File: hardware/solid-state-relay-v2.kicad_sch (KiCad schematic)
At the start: 17 parts

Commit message: fix schematic library
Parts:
- C1: value (none) -> 220pF; footprint (none) -> kicad-libraries:C0402F; symbol C -> tinkerforge:C
- C2: value (none) -> 10uF; footprint (none) -> kicad-libraries:C0805; symbol C -> tinkerforge:C
- C3: value (none) -> 1uF; footprint (none) -> kicad-libraries:C0603F; symbol C -> tinkerforge:C
- C4: value (none) -> 100nF; footprint (none) -> kicad-libraries:C0603F; symbol C -> tinkerforge:C
- D1: value (none) -> blue; footprint (none) -> kicad-libraries:D0603F; symbol LED -> tinkerforge:LED
- P1: value (none) -> CON-SENSOR2; footprint (none) -> kicad-libraries:CON-SENSOR2; symbol CON-SENSOR2 -> tinkerforge:CON-SENSOR2
- P2, P3: value (none) -> TST; footprint (none) -> kicad-libraries:Drill; symbol TST -> tinkerforge:TST
- P5: value (none) -> BOOT; footprint (none) -> kicad-libraries:SolderJumper; symbol CONN_01X02 -> tinkerforge:CONN_01X02
- Q1: value (none) -> 2N7002P; footprint (none) -> kicad-libraries:SOT23GDS; symbol MOSFET_N_CH -> tinkerforge:MOSFET_N_CH
- R1: value (none) -> 10k; footprint (none) -> kicad-libraries:R0603F; symbol R -> tinkerforge:R
- R2, R3: value (none) -> 1k; footprint (none) -> kicad-libraries:R0603F; symbol R -> tinkerforge:R
- RP1: value (none) -> 82; footprint (none) -> kicad-libraries:4X0402; symbol R_PACK4 -> tinkerforge:R_PACK4
- U1: value (none) -> XMC110024; footprint (none) -> kicad-libraries:QFN24-4x4mm-0.5mm; symbol XMC1XXX24 -> tinkerforge:XMC1XXX24
- U2, U3: value (none) -> DRILL; footprint (none) -> kicad-libraries:DRILL_NP; symbol DRILL -> tinkerforge:DRILL
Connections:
- net S-CLK: now also RP1.7 (R2), U1.23 (P0.14_IO)
- net S-CS: now also RP1.8 (R1), U1.22 (P0.13_IO)
- net S-MISO: now also RP1.5 (R4), U1.1 (P2.0_AIO)
- net S-MOSI: now also RP1.6 (R3), U1.24 (P0.15_IO)
- net SSR: now also Q1.G, U1.13 (P1.1_IHO)
- new net: Q1.D, R2.2
- new net: P1.4, RP1.1 (P1)
- new net: P1.5, RP1.2 (P2)
- new net: P1.6, RP1.3 (P3)
- new net: C1.1, P1.7, RP1.4 (P4)
- new net: R3.1, U1.15 (P0.0_IO)
- new net: P5.2 (P2), U1.4 (P2.6_AI)
- new net: D1.2 (K), R3.2
- new net +5V: P1.1, R2.1
- new net GND: C1.2, C2.2, C3.2, C4.2, P1.2, P1.EP, P5.1 (P1), Q1.S, R1.2, U1.9 (VSSP/VSS), U1.EXP (VSSP)
- new net VCC: C2.1, C3.1, C4.1, D1.1 (A), P1.3, U1.10 (VDDP/VDD)

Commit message: Hardware 2.1: Made Pcb bigger to fit on the 40mm grid. Data Cleanup
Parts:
- P2: renamed from P3; symbol tinkerforge:TST -> tinkerforge:CONN_1
- P3: renamed from P2; symbol tinkerforge:TST -> tinkerforge:CONN_1
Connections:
- net +5V: now also P2.1
- net SSR: now also R1.1
- net at Q1.D, R2.2: now also P3.1
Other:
- note added: "Copyright Tinkerforge GmbH 2023. This documentation describes Open Hardware and is licensed under the CERN OHL v. 1.1. You may redistribute and modify this documentation under the terms of the CERN OHL v.1.1. (http://ohwr.org/cernohl). This documentation is distributed WITHOUT ANY EXPRESS OR IMPLIED WARRANTY, INCLUDING OF MERCHANTABILITY, SATISFACTORY QUALITY AND FITNESS FOR A PARTICULAR PURPOSE.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"
- note removed: "Copyright Tinkerforge GmbH 2017. This documentation describes Open Hardware and is licensed under the CERN OHL v. 1.1. You may redistribute and modify this documentation under the terms of the CERN OHL v.1.1. (http://ohwr.org/cernohl). This documentation is distributed WITHOUT ANY EXPRESS OR IMPLIED WARRANTY, INCLUDING OF MERCHANTABILITY, SATISFACTORY QUALITY AND FITNESS FOR A PARTICULAR PURPOSE.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"
- moved on the sheet: R1
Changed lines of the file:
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@@
   (title_block
     (title "Solid State Relay Bricklet")
-    (date "2017-09-18")
-    (rev "2.0")
+    (date "2023-01-27")
+    (rev "2.1")
     (company "Tinkerforge GmbH")
     (comment 1 "Licensed under CERN OHL v.1.1")
-    (comment 2 "Copyright (©) 2017, L.Lauer <lukas@tinkerforge.com>")
+    (comment 2 "Copyright (©) 2023, T.Schneidermann <tim@tinkerforge.com>")
   )
   (junction (at 57.15 20.32) (diameter 0) (color 0 0 0 0)
@@
   )
   (junction (at 40.64 45.72) (diameter 0) (color 0 0 0 0)
+  )
+  (junction (at 223.52 96.52) (diameter 0) (color 0 0 0 0)
   )
   (junction (at 100.33 181.61) (diameter 0) (color 0 0 0 0)
@@
     (stroke (width 0) (type default) (color 0 0 0 0))
   )
-  (wire (pts (xy 212.09 96.52) (xy 240.03 96.52))
+  (wire (pts (xy 212.09 96.52) (xy 223.52 96.52))
     (stroke (width 0) (type default) (color 0 0 0 0))
   )
@@
     (stroke (width 0) (type default) (color 0 0 0 0))
   )
-  (wire (pts (xy 224.79 110.49) (xy 224.79 109.22))
+  (wire (pts (xy 223.52 110.49) (xy 223.52 109.22))
     (stroke (width 0) (type default) (color 0 0 0 0))
   )
@@
     (stroke (width 0) (type default) (color 0 0 0 0))
   )
-  (wire (pts (xy 254 91.44) (xy 254 85.09))
+  (wire (pts (xy 254 91.44) (xy 254 87.63))
     (stroke (width 0) (type default) (color 0 0 0 0))
   )
@@
   )
   (wire (pts (xy 57.15 20.32) (xy 57.15 21.59))
+    (stroke (width 0) (type default) (color 0 0 0 0))
+  )
+  (wire (pts (xy 223.52 96.52) (xy 240.03 96.52))
     (stroke (width 0) (type default) (color 0 0 0 0))
   )
@@
     (effects (font (size 1.1938 1.1938)) (justify left bottom))
   )
-  (text "Copyright Tinkerforge GmbH 2017.\nThis documentation describes Open Hardware and is licensed under the\nCERN OHL v. 1.1.\nYou may redistribute and modify this documentation under the terms of the\nCERN OHL v.1.1. (http://ohwr.org/cernohl). This documentation is distributed\nWITHOUT ANY EXPRESS OR IMPLIED WARRANTY, INCLUDING OF\nMERCHANTABILITY, SATISFACTORY QUALITY AND FITNESS FOR A\nPARTICULAR PURPOSE. Please see the CERN OHL v.1.1 for applicable\nconditions\n"
+  (text "Copyright Tinkerforge GmbH 2023.\nThis documentation describes Open Hardware and is licensed under the\nCERN OHL v. 1.1.\nYou may redistribute and modify this documentation under the terms of the\nCERN OHL v.1.1. (http://ohwr.org/cernohl). This documentation is distributed\nWITHOUT ANY EXPRESS OR IMPLIED WARRANTY, INCLUDING OF\nMERCHANTABILITY, SATISFACTORY QUALITY AND FITNESS FOR A\nPARTICULAR PURPOSE. Please see the CERN OHL v.1.1 for applicable\nconditions\n"
     (at 12.7 196.85 0)
     (effects (font (size 1.016 1.016)) (justify left bottom))
@@
     (pin "1")
   )
-  (symbol (lib_id "tinkerforge:R") (at 224.79 102.87 0) (unit 1)
-    (in_bom yes) (on_board yes)
-    (property "Reference" "R1" (id 0) (at 226.822 102.87 90))
-    (property "Value" "10k" (id 1) (at 224.79 102.87 90))
-    (property "Footprint" "kicad-libraries:R0603F" (id 2) (at 224.79 102.87 0)
-      (effects (font (size 1.524 1.524)) hide)
-    )
-    (property "Datasheet" "" (id 3) (at 224.79 102.87 0)
-      (effects (font (size 1.524 1.524)))
-    )
-    (pin "1")
-    (pin "2")
-  )
-  (symbol (lib_id "tinkerforge:GND") (at 224.79 110.49 0) (unit 1)
-    (in_bom yes) (on_board yes)
-    (property "Reference" "#PWR05" (id 0) (at 224.79 110.49 0)
-      (effects (font (size 0.762 0.762)) hide)
-    )
-    (property "Value" "GND" (id 1) (at 224.79 112.268 0)
-      (effects (font (size 0.762 0.762)) hide)
-    )
-    (property "Footprint" "" (id 2) (at 224.79 110.49 0)
-      (effects (font (size 1.524 1.524)) hide)
-    )
-    (property "Datasheet" "" (id 3) (at 224.79 110.49 0)
+  (symbol (lib_id "tinkerforge:R") (at 223.52 102.87 0) (unit 1)
+    (in_bom yes) (on_board yes)
+    (property "Reference" "R1" (id 0) (at 225.552 102.87 90))
+    (property "Value" "10k" (id 1) (at 223.52 102.87 90))
+    (property "Footprint" "kicad-libraries:R0603F" (id 2) (at 223.52 102.87 0)
+      (effects (font (size 1.524 1.524)) hide)
+    )
+    (property "Datasheet" "" (id 3) (at 223.52 102.87 0)
+      (effects (font (size 1.524 1.524)))
+    )
+    (pin "1")
+    (pin "2")
+  )
+  (symbol (lib_id "tinkerforge:GND") (at 223.52 110.49 0) (unit 1)
+    (in_bom yes) (on_board yes)
+    (property "Reference" "#PWR05" (id 0) (at 223.52 110.49 0)
+      (effects (font (size 0.762 0.762)) hide)
+    )
+    (property "Value" "GND" (id 1) (at 223.52 112.268 0)
+      (effects (font (size 0.762 0.762)) hide)
+    )
+    (property "Footprint" "" (id 2) (at 223.52 110.49 0)
+      (effects (font (size 1.524 1.524)) hide)
+    )
+    (property "Datasheet" "" (id 3) (at 223.52 110.49 0)
       (effects (font (size 1.524 1.524)) hide)
     )
@@
     (pin "2")
   )
-  (symbol (lib_id "tinkerforge:TST") (at 254 85.09 270) (unit 1)
-    (in_bom yes) (on_board yes)
-    (property "Reference" "P2" (id 0) (at 261.62 85.09 0)
+  (symbol (lib_id "tinkerforge:CONN_1") (at 256.54 87.63 0) (unit 1)
+    (in_bom yes) (on_board yes)
+    (property "Reference" "P3" (id 0) (at 260.35 87.63 0)
       (effects (font (size 1.016 1.016)))
     )
-    (property "Value" "TST" (id 1) (at 260.35 85.09 0)
+    (property "Value" "TST" (id 1) (at 260.35 86.36 0)
       (effects (font (size 0.762 0.762)))
     )
-    (property "Footprint" "kicad-libraries:Drill" (id 2) (at 254 85.09 0)
-      (effects (font (size 1.524 1.524)) hide)
-    )
-    (property "Datasheet" "" (id 3) (at 254 85.09 0)
-      (effects (font (size 1.524 1.524)))
-    )
-  )
-  (symbol (lib_id "tinkerforge:TST") (at 254 82.55 270) (unit 1)
-    (in_bom yes) (on_board yes)
-    (property "Reference" "P3" (id 0) (at 261.62 82.55 0)
+    (property "Footprint" "kicad-libraries:Drill" (id 2) (at 256.54 87.63 0)
+      (effects (font (size 1.524 1.524)) hide)
+    )
+    (property "Datasheet" "" (id 3) (at 256.54 87.63 0)
+      (effects (font (size 1.524 1.524)))
+    )
+    (pin "1")
+  )
+  (symbol (lib_id "tinkerforge:CONN_1") (at 256.54 82.55 0) (unit 1)
+    (in_bom yes) (on_board yes)
+    (property "Reference" "P2" (id 0) (at 260.35 82.55 0)
       (effects (font (size 1.016 1.016)))
     )
-    (property "Value" "TST" (id 1) (at 260.35 82.55 0)
+    (property "Value" "TST" (id 1) (at 260.35 83.82 0)
       (effects (font (size 0.762 0.762)))
     )
-    (property "Footprint" "kicad-libraries:Drill" (id 2) (at 254 82.55 0)
-      (effects (font (size 1.524 1.524)) hide)
-    )
-    (property "Datasheet" "" (id 3) (at 254 82.55 0)
-      (effects (font (size 1.524 1.524)))
-    )
+    (property "Footprint" "kicad-libraries:Drill" (id 2) (at 256.54 82.55 0)
+      (effects (font (size 1.524 1.524)) hide)
+    )
+    (property "Datasheet" "" (id 3) (at 256.54 82.55 0)
+      (effects (font (size 1.524 1.524)))
+    )
+    (pin "1")
   )
   (symbol (lib_id "tinkerforge:CON-SENSOR2") (at 27.94 38.1 0) (mirror y) (unit 1)
@@
       (reference "P1") (unit 1) (value "CON-SENSOR2") (footprint "kicad-libraries:CON-SENSOR2")
     )
+    (path "/00000000-0000-0000-0000-0000537f4fb9"
+      (reference "P2") (unit 1) (value "TST") (footprint "kicad-libraries:Drill")
+    )
     (path "/00000000-0000-0000-0000-0000537f4fac"
-      (reference "P2") (unit 1) (value "TST") (footprint "kicad-libraries:Drill")
-    )
-    (path "/00000000-0000-0000-0000-0000537f4fb9"
       (reference "P3") (unit 1) (value "TST") (footprint "kicad-libraries:Drill")
     )

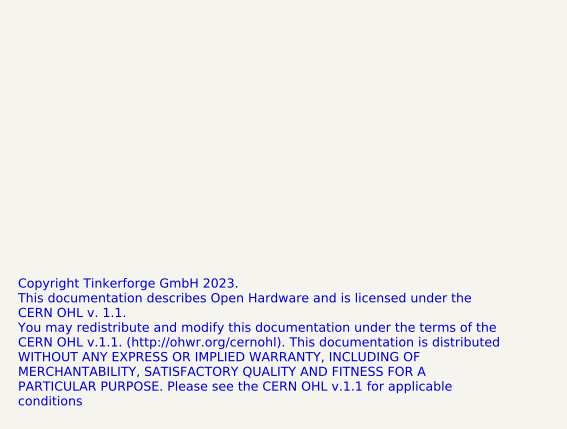
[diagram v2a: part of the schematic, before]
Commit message: version 2.2: add slotted holes
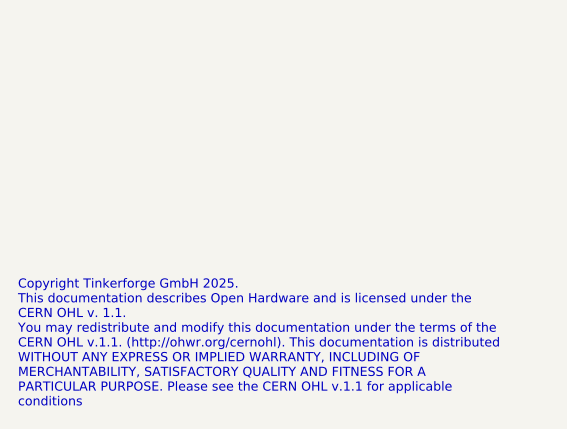
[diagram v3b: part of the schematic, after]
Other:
- note added: "Copyright Tinkerforge GmbH 2025. This documentation describes Open Hardware and is licensed under the CERN OHL v. 1.1. You may redistribute and modify this documentation under the terms of the CERN OHL v.1.1. (http://ohwr.org/cernohl). This documentation is distributed WITHOUT ANY EXPRESS OR IMPLIED WARRANTY, INCLUDING OF MERCHANTABILITY, SATISFACTORY QUALITY AND FITNESS FOR A PARTICULAR PURPOSE.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"
- note removed: "Copyright Tinkerforge GmbH 2023. This documentation describes Open Hardware and is licensed under the CERN OHL v. 1.1. You may redistribute and modify this documentation under the terms of the CERN OHL v.1.1. (http://ohwr.org/cernohl). This documentation is distributed WITHOUT ANY EXPRESS OR IMPLIED WARRANTY, INCLUDING OF MERCHANTABILITY, SATISFACTORY QUALITY AND FITNESS FOR A PARTICULAR PURPOSE.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"
